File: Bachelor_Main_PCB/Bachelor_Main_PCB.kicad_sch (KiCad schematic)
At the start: 3 parts, among them J1 F32Q-1A7H1-11022, U1 SC0683

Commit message: Add GND to RPI CM
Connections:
- net GND: now also U1.1 (GND), U1.107 (GND), U1.108 (GND), U1.113 (GND), U1.114 (GND), U1.119 (GND), U1.120 (GND), U1.125 (GND), U1.126 (GND), U1.13 (GND), U1.131 (GND), U1.132 (GND), U1.137 (GND), U1.138 (GND), U1.14 (GND), U1.144 (GND), U1.150 (GND), U1.155 (GND), U1.156 (GND), U1.161 (GND), U1.162 (GND), U1.167 (GND), U1.168 (GND), U1.173 (GND), U1.174 (GND), U1.179 (GND), U1.180 (GND), U1.185 (GND), U1.186 (GND), U1.191 (GND), U1.192 (GND), U1.197 (GND), U1.198 (GND), U1.2 (GND), U1.22 (GND), U1.23 (GND), U1.32 (GND), U1.33 (GND), U1.42 (GND), U1.43 (GND), U1.52 (GND), U1.53 (GND), U1.59 (GND), U1.60 (GND), U1.65 (GND), U1.66 (GND), U1.7 (GND), U1.71 (GND), U1.74 (GND), U1.8 (GND), U1.98 (GND), U1.SH1 (MOUNTING_PADS), U1.SH2 (MOUNTING_PADS), U1.SH3 (MOUNTING_PADS), U1.SH4 (MOUNTING_PADS)
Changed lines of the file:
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@@
+	)
+	(symbol
+		(lib_id "power:GND")
+		(at 119.38 139.7 0)
+		(unit 1)
+		(exclude_from_sim no)
+		(in_bom yes)
+		(on_board yes)
+		(dnp no)
+		(fields_autoplaced yes)
+		(property "Reference" "#PWR03"
+			(at 119.38 146.05 0)
+			(effects
+				(font
+					(size 1.27 1.27)
+				)
+				(hide yes)
+			)
+		)
+		(property "Value" "GND"
+			(at 119.38 144.78 0)
+			(effects
+				(font
+					(size 1.27 1.27)
+				)
+			)
+		)
+		(property "Footprint" ""
+			(at 119.38 139.7 0)
+			(effects
+				(font
+					(size 1.27 1.27)
+				)
+				(hide yes)
+			)
+		)
+		(property "Datasheet" ""
+			(at 119.38 139.7 0)
+			(effects
+				(font
+					(size 1.27 1.27)
+				)
+				(hide yes)
+			)
+		)
+		(property "Description" "Power symbol creates a global label with name \"GND\" , ground"
+			(at 119.38 139.7 0)
+			(effects
+				(font
+					(size 1.27 1.27)
+				)
+				(hide yes)
+			)
+		)
+		(pin "1"
+		)
+		(instances
+			(project ""
+				(path "/3544d663-329e-4884-b753-28436ca187e8"
+					(reference "#PWR03")
+					(unit 1)
+				)
+			)
+		)
 	)
 	(symbol
@@
 					(unit 1)
 				)
+			)
+		)
+	)
+	(symbol
+		(lib_id "power:GND")
+		(at 180.34 139.7 0)
+		(unit 1)
+		(exclude_from_sim no)
+		(in_bom yes)
+		(on_board yes)
+		(dnp no)
+		(fields_autoplaced yes)
+		(property "Reference" "#PWR04"
+			(at 180.34 146.05 0)
+			(effects
+				(font
+					(size 1.27 1.27)
+				)
+				(hide yes)
+			)
+		)
+		(property "Value" "GND"
+			(at 180.34 144.78 0)
+			(effects
+				(font
+					(size 1.27 1.27)
+				)
+			)
+		)
+		(property "Footprint" ""
+			(at 180.34 139.7 0)
+			(effects
+				(font
+					(size 1.27 1.27)
+				)
+				(hide yes)
+			)
+		)
+		(property "Datasheet" ""
+			(at 180.34 139.7 0)
+			(effects
+				(font
+					(size 1.27 1.27)
+				)
+				(hide yes)
+			)
+		)
+		(property "Description" "Power symbol creates a global label with name \"GND\" , ground"
+			(at 180.34 139.7 0)
+			(effects
+				(font
+					(size 1.27 1.27)
+				)
+				(hide yes)
+			)
+		)
+		(pin "1"
+		)
+		(instances
+			(project ""
+				(path "/3544d663-329e-4884-b753-28436ca187e8"
+					(reference "#PWR04")
+					(unit 1)
+				)

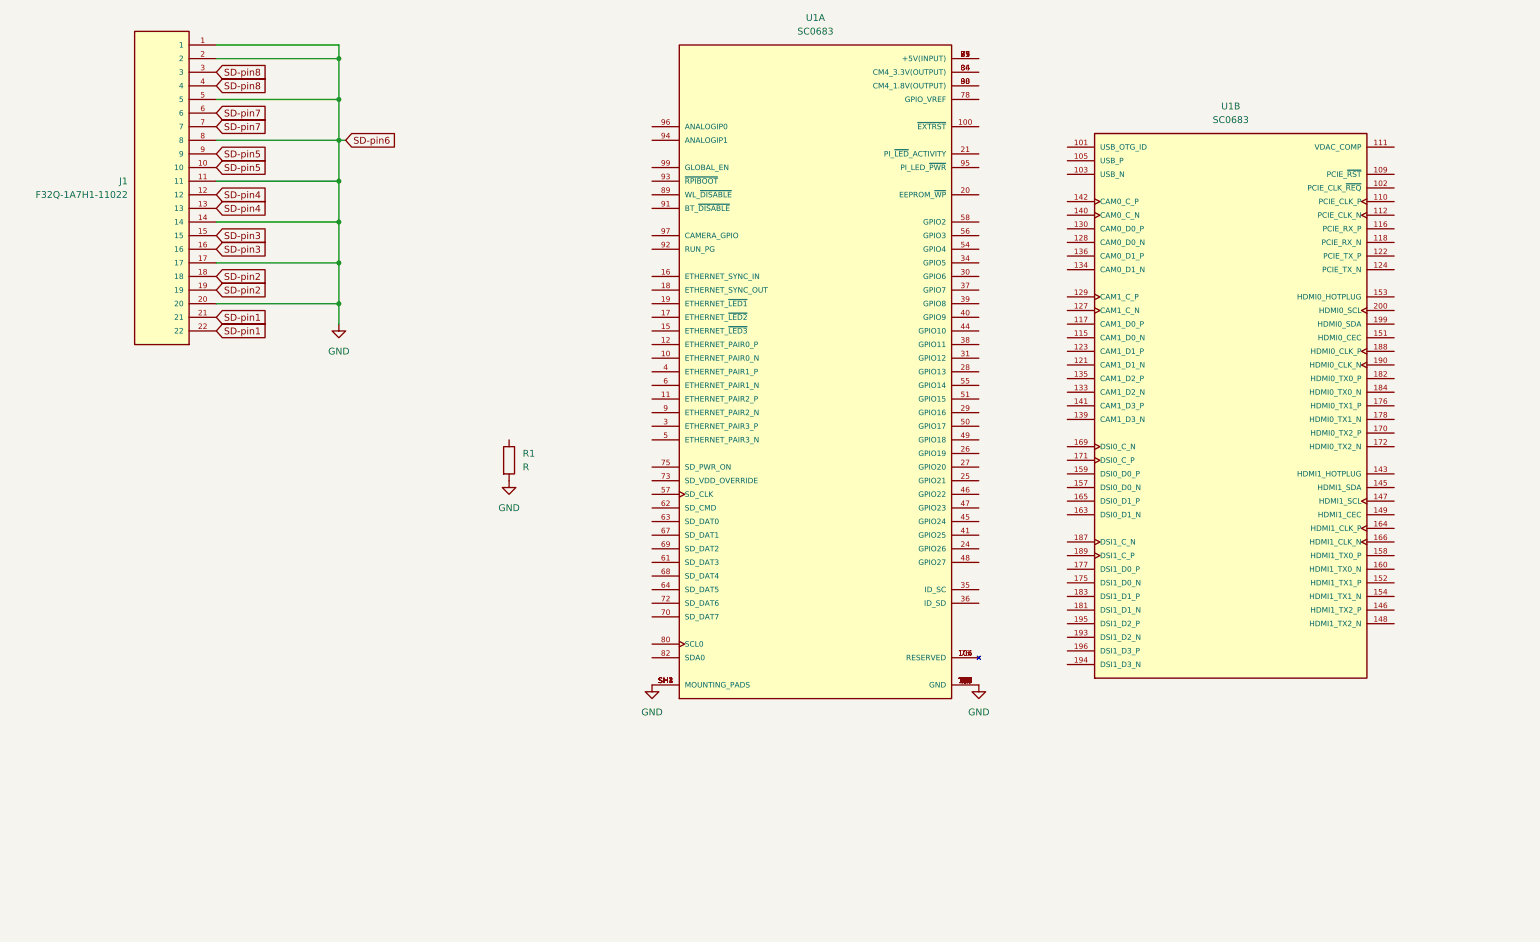
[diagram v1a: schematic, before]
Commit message: Add Spacers for RPI CM and created separate hierarchical sheets
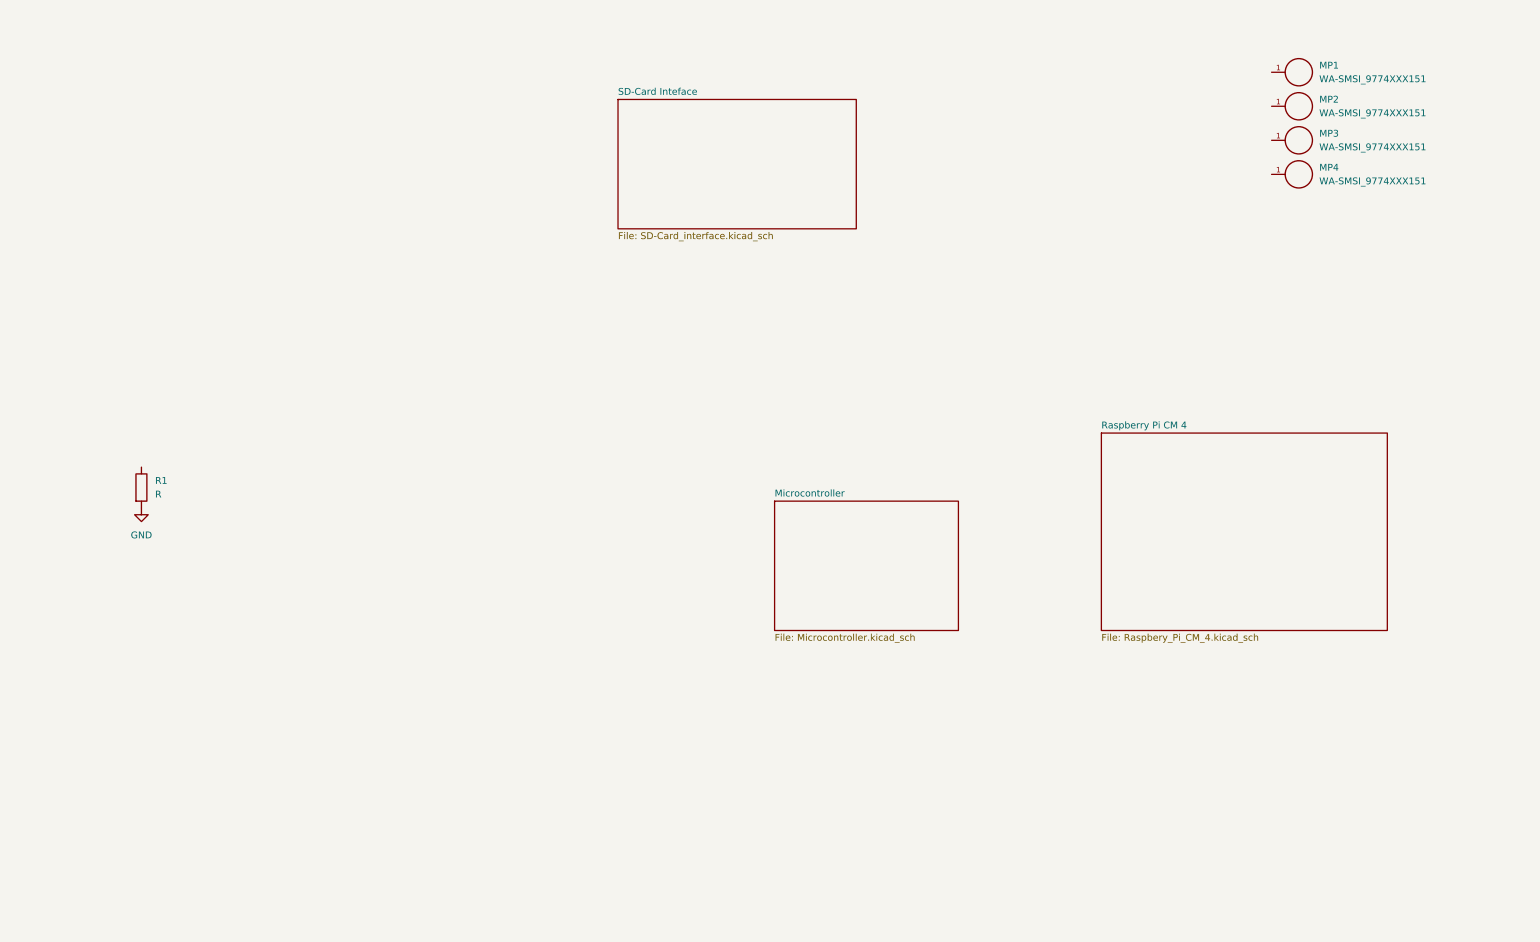
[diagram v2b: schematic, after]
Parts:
- removed J1: F32Q-1A7H1-11022, F32Q-1A7H1-11022:AMPHENOL_F32Q-1A7H1-11022, symbol F32Q-1A7H1-11022:F32Q-1A7H1-11022
- removed U1: SC0683, SC0683:MODULE_SC0683, symbol SC0683:SC0683
- added MP1, MP2, MP3, MP4: WA-SMSI_9774XXX151, WA-SMSI_9774XXX151:WA-SMSI_9774030151, symbol WA-SMSI_9774XXX151:WA-SMSI_9774XXX151
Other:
- added sheet Microcontroller (Microcontroller.kicad_sch)
- added sheet Raspberry Pi CM 4 (Raspbery_Pi_CM_4.kicad_sch)
- added sheet SD-Card Inteface (SD-Card_interface.kicad_sch)
- moved on the sheet: R1

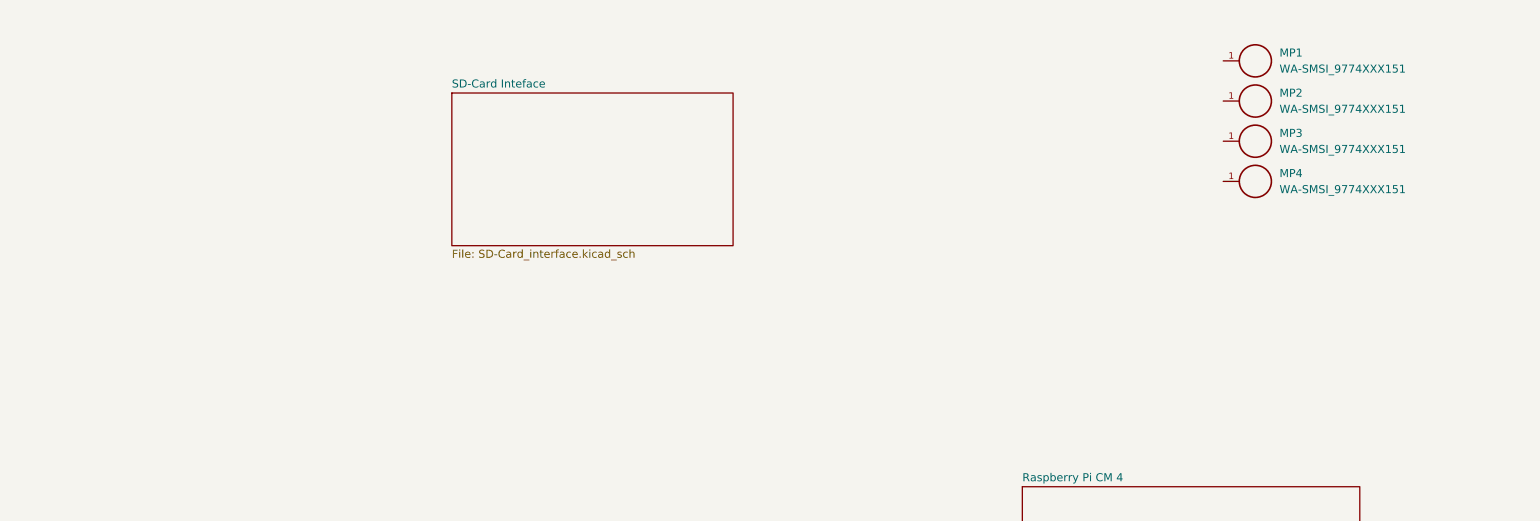
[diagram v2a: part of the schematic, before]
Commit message: Add Sierra Wireless modem and 100pin RPI CM connectors
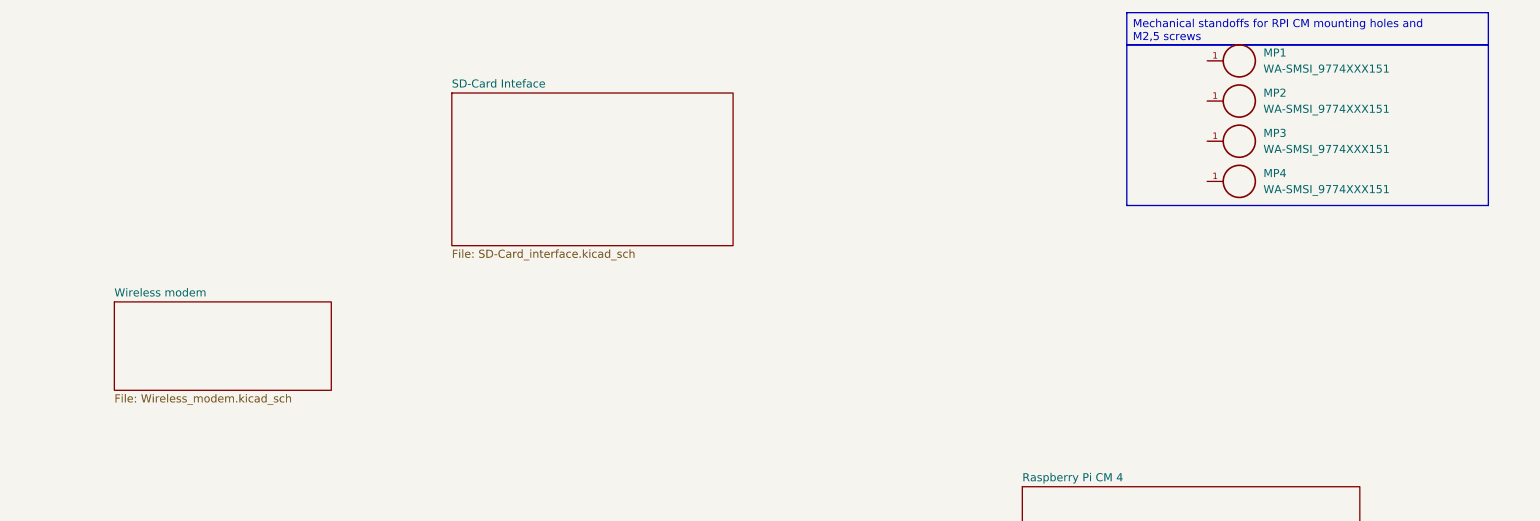
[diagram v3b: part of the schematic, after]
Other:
- added sheet Wireless modem (Wireless_modem.kicad_sch)
- moved on the sheet: MP1, MP2, MP3, MP4

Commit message: Small changes
Just moved some components
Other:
- added sheet Power supply (Power_supply.kicad_sch)
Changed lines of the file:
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@@
 	)
 	(sheet
-		(at 59.69 63.5)
+		(at 45.72 102.87)
 		(size 34.29 13.97)
 		(exclude_from_sim no)
@@
 		)
 		(property "Sheetname" "Wireless modem"
-			(at 59.69 62.7884 0)
+			(at 45.72 102.1584 0)
 			(effects
 				(font
@@
 		)
 		(property "Sheetfile" "Wireless_modem.kicad_sch"
-			(at 59.69 78.0546 0)
+			(at 45.72 117.4246 0)
 			(effects
 				(font
@@
 	)
 	(sheet
-		(at 203.2 92.71)
+		(at 203.2 74.93)
 		(size 53.34 36.83)
 		(exclude_from_sim no)
@@
 		)
 		(property "Sheetname" "Raspberry Pi CM 4"
-			(at 203.2 91.9984 0)
+			(at 203.2 74.2184 0)
 			(effects
 				(font
@@
 		)
 		(property "Sheetfile" "Raspbery_Pi_CM_4.kicad_sch"
-			(at 203.2 130.1246 0)
+			(at 203.2 112.3446 0)
 			(effects
 				(font
@@
 	)
 	(sheet
-		(at 142.24 105.41)
-		(size 34.29 24.13)
+		(at 64.77 127)
+		(size 46.99 40.64)
+		(exclude_from_sim no)
+		(in_bom yes)
+		(on_board yes)
+		(dnp no)
+		(fields_autoplaced yes)
+		(stroke
+			(width 0.1524)
+			(type solid)
+		)
+		(fill
+			(color 0 0 0 0.0000)
+		)
+		(property "Sheetname" "Power supply"
+			(at 64.77 126.2884 0)
+			(effects
+				(font
+					(size 1.27 1.27)
+				)
+				(justify left bottom)
+			)
+		)
+		(property "Sheetfile" "Power_supply.kicad_sch"
+			(at 64.77 168.2246 0)
+			(effects
+				(font
+					(size 1.27 1.27)
+				)
+				(justify left top)
+			)
+		)
+		(instances
+			(project "Bachelor_Main_PCB"
+				(path "/3544d663-329e-4884-b753-28436ca187e8"
+					(page "6")
+				)
+			)
+		)
+	)
+	(sheet
+		(at 111.76 50.8)
+		(size 53.34 54.61)
 		(exclude_from_sim no)
 		(in_bom yes)
@@
 		)
 		(property "Sheetname" "Microcontroller"
-			(at 142.24 104.6984 0)
+			(at 111.76 50.0884 0)
 			(effects
 				(font
@@
 		)
 		(property "Sheetfile" "Microcontroller.kicad_sch"
-			(at 142.24 130.1246 0)
+			(at 111.76 105.9946 0)
 			(effects
 				(font
@@
 	)
 	(sheet
-		(at 113.03 30.48)
+		(at 35.56 19.05)
 		(size 44.45 24.13)
 		(exclude_from_sim no)
@@
 		)
 		(property "Sheetname" "SD-Card Inteface"
-			(at 113.03 29.7684 0)
+			(at 35.56 18.3384 0)
 			(effects
 				(font
@@
 		)
 		(property "Sheetfile" "SD-Card_interface.kicad_sch"
-			(at 113.03 55.1946 0)
+			(at 35.56 43.7646 0)
 			(effects
 				(font

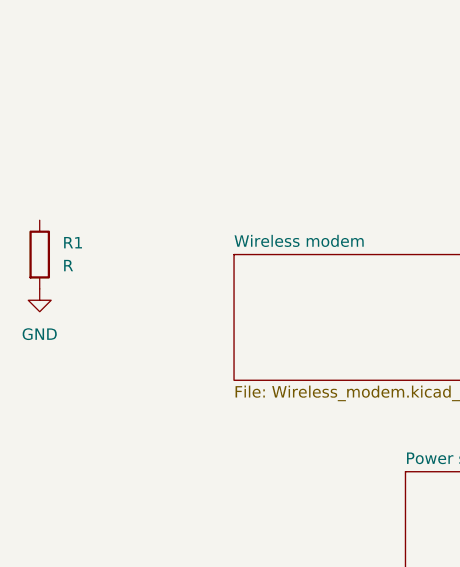
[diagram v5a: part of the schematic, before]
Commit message: Route ID pin on USB3320, Fix 0603 footprint on resistors
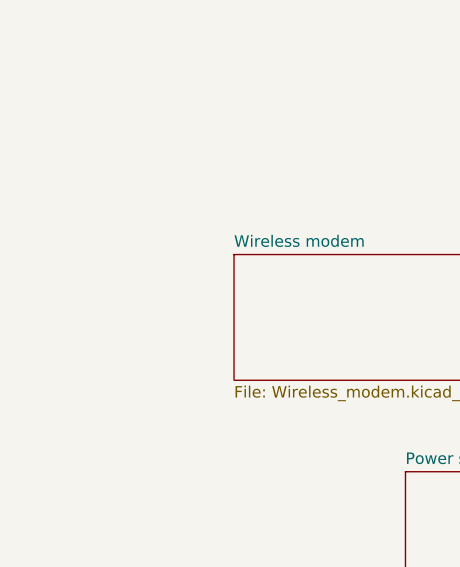
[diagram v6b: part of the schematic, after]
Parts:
- removed R1: R, Resistor_SMD:R_0201_0603Metric, symbol Device:R
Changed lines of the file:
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@@
-	)
-	(symbol
-		(lib_id "power:GND")
-		(at 24.13 106.68 0)
-		(unit 1)
-		(exclude_from_sim no)
-		(in_bom yes)
-		(on_board yes)
-		(dnp no)
-		(fields_autoplaced yes)
-		(property "Reference" "#PWR01"
-			(at 24.13 113.03 0)
-			(effects
-				(font
-					(size 1.27 1.27)
-				)
-				(hide yes)
-			)
-		)
-		(property "Value" "GND"
-			(at 24.13 111.76 0)
-			(effects
-				(font
-					(size 1.27 1.27)
-				)
-			)
-		)
-		(property "Footprint" ""
-			(at 24.13 106.68 0)
-			(effects
-				(font
-					(size 1.27 1.27)
-				)
-				(hide yes)
-			)
-		)
-		(property "Datasheet" ""
-			(at 24.13 106.68 0)
-			(effects
-				(font
-					(size 1.27 1.27)
-				)
-				(hide yes)
-			)
-		)
-		(property "Description" "Power symbol creates a global label with name \"GND\" , ground"
-			(at 24.13 106.68 0)
-			(effects
-				(font
-					(size 1.27 1.27)
-				)
-				(hide yes)
-			)
-		)
-		(pin "1"
-		)
-		(instances
-			(project ""
-				(path "/3544d663-329e-4884-b753-28436ca187e8"
-					(reference "#PWR01")
-					(unit 1)
-				)
-			)
-		)
 	)
 	(symbol
@@
 					(unit 1)
 				)
-			)
-		)
-	)
-	(symbol
-		(lib_id "Device:R")
-		(at 24.13 102.87 0)
-		(unit 1)
-		(exclude_from_sim no)
-		(in_bom yes)
-		(on_board yes)
-		(dnp no)
-		(fields_autoplaced yes)
-		(property "Reference" "R1"
-			(at 26.67 101.5999 0)
-			(effects
-				(font
-					(size 1.27 1.27)
-				)
-				(justify left)
-			)
-		)
-		(property "Value" "R"
-			(at 26.67 104.1399 0)
-			(effects
-				(font
-					(size 1.27 1.27)
-				)
-				(justify left)
-			)
-		)
-		(property "Footprint" "Resistor_SMD:R_0201_0603Metric"
-			(at 22.352 102.87 90)
-			(effects
-				(font
-					(size 1.27 1.27)
-				)
-				(hide yes)
-			)
-		)
-		(property "Datasheet" "~"
-			(at 24.13 102.87 0)
-			(effects
-				(font
-					(size 1.27 1.27)
-				)
-				(hide yes)
-			)
-		)
-		(property "Description" "Resistor"
-			(at 24.13 102.87 0)
-			(effects
-				(font
-					(size 1.27 1.27)
-				)
-				(hide yes)
-			)
-		)
-		(pin "2"
-		)
-		(pin "1"
-		)
-		(instances
-			(project ""
-				(path "/3544d663-329e-4884-b753-28436ca187e8"
-					(reference "R1")
-					(unit 1)
-				)
